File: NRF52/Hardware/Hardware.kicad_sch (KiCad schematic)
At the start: 66 parts, among them J1 USB_C_Receptacle_USB2.0, J2 BAT, J2 LCD, J2 MOTOR, J3 PROG, Q1 AO3401A, Q2 AO3400A, SW1 SW_Push, SW2 SW_Push, SW3 SW_Push, U1 nRF52840, U3 MAX17048, U3 TP4054, U4 XC6206PxxxMR, U5 LSM6DS3, U6 DS3231MZ, U7 W25Q128JVS, Y1 32MHz 8pF ±10ppm, Y2 32.768kHz 6pF ±20ppm

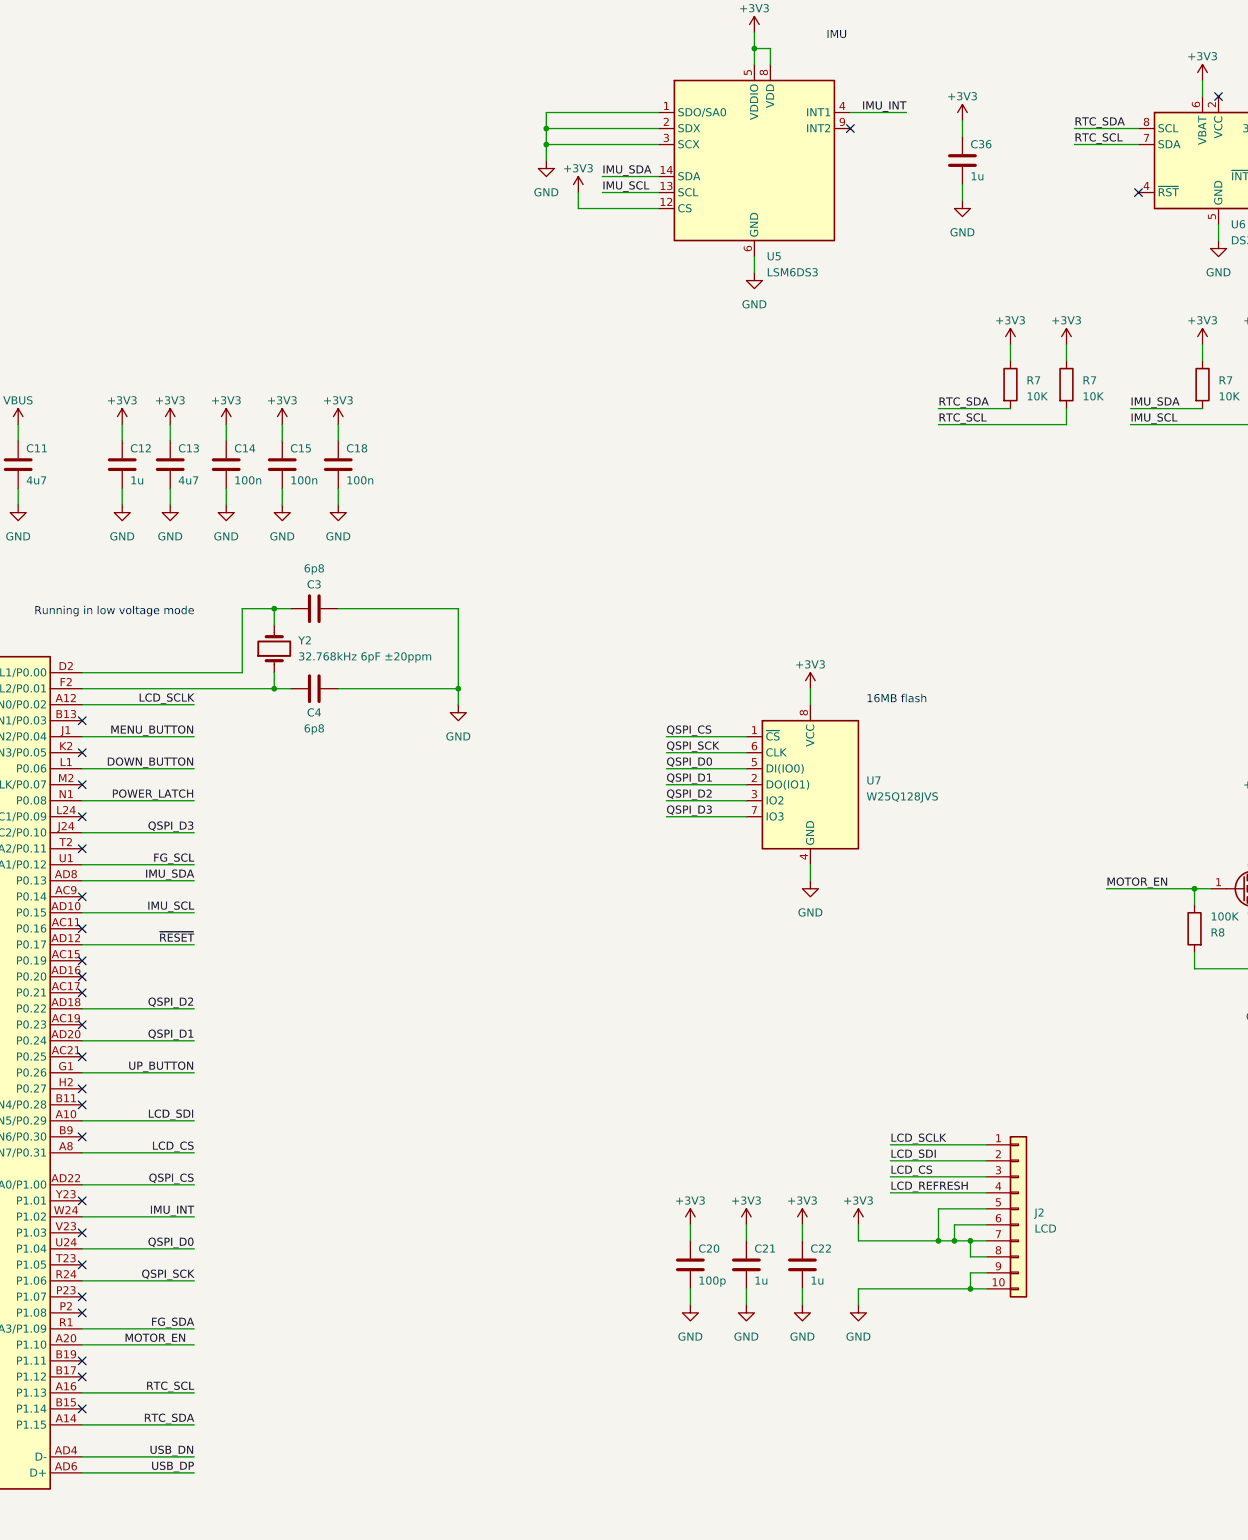
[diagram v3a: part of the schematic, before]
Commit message: Start circuitpython version of software
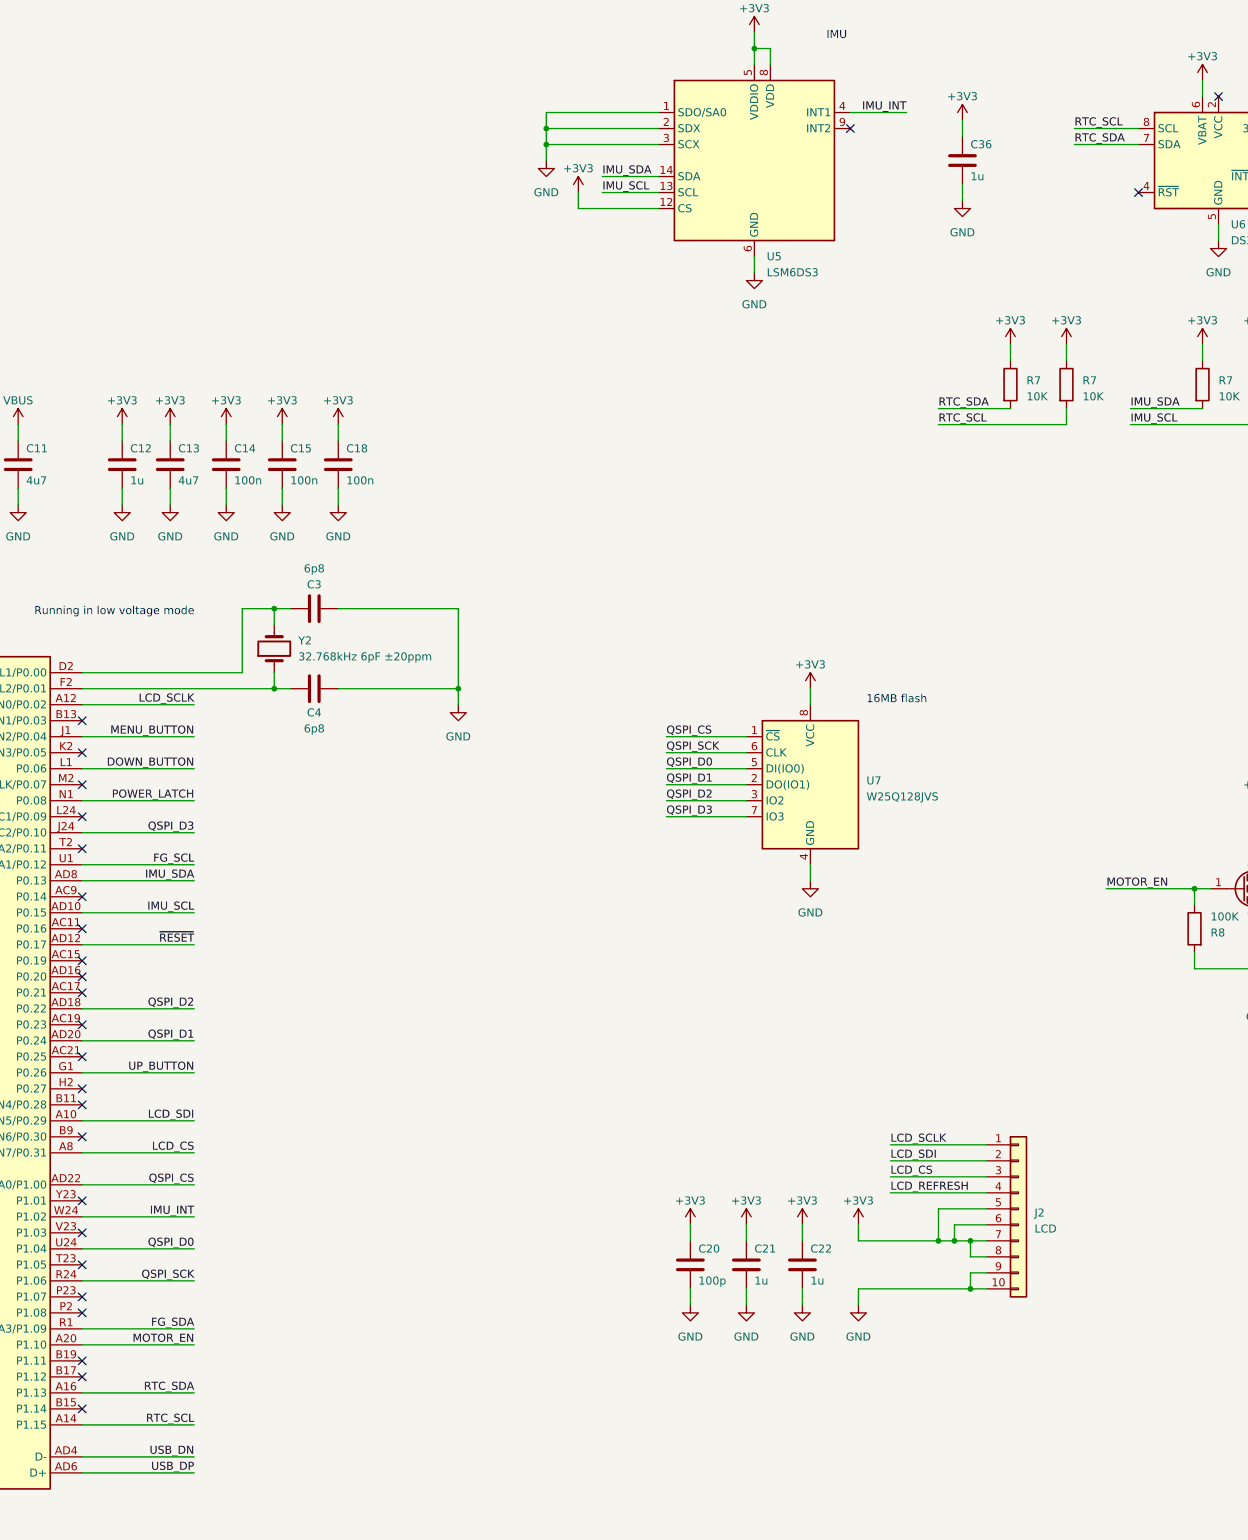
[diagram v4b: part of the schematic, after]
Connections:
- net RTC_SCL: now also U1.A14 (P1.15), U6.8 (SCL); no longer U1.A16 (P1.13), U6.7 (SDA)
- net RTC_SDA: now also U1.A16 (P1.13), U6.7 (SDA); no longer U1.A14 (P1.15), U6.8 (SCL)
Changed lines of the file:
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@@
-    (effects (font (size 1.27 1.27)) (justify left bottom))
-  )
-  (label "RTC_SCL" (at 466.09 123.19 0) (fields_autoplaced)
     (effects (font (size 1.27 1.27)) (justify left bottom))
   )
@@
     (effects (font (size 1.27 1.27)) (justify left bottom))
   )
+  (label "RTC_SDA" (at 326.39 321.31 180) (fields_autoplaced)
+    (effects (font (size 1.27 1.27)) (justify right bottom))
+  )
   (label "MENU_BUTTON" (at 326.39 217.17 180) (fields_autoplaced)
     (effects (font (size 1.27 1.27)) (justify right bottom))
@@
     (effects (font (size 1.27 1.27)) (justify right bottom))
   )
+  (label "RTC_SDA" (at 466.09 123.19 0) (fields_autoplaced)
+    (effects (font (size 1.27 1.27)) (justify left bottom))
+  )
   (label "QSPI_D0" (at 326.39 298.45 180) (fields_autoplaced)
     (effects (font (size 1.27 1.27)) (justify right bottom))
-  )
-  (label "RTC_SDA" (at 466.09 120.65 0) (fields_autoplaced)
-    (effects (font (size 1.27 1.27)) (justify left bottom))
   )
   (label "USB_DN" (at 71.12 41.91 180) (fields_autoplaced)
@@
     (effects (font (size 1.27 1.27)) (justify right bottom))
   )
+  (label "RTC_SCL" (at 466.09 120.65 0) (fields_autoplaced)
+    (effects (font (size 1.27 1.27)) (justify left bottom))
+  )
   (label "UP_BUTTON" (at 326.39 270.51 180) (fields_autoplaced)
     (effects (font (size 1.27 1.27)) (justify right bottom))
@@
     (effects (font (size 1.27 1.27)) (justify right bottom))
   )
-  (label "RTC_SCL" (at 326.39 321.31 180) (fields_autoplaced)
-    (effects (font (size 1.27 1.27)) (justify right bottom))
-  )
   (label "DOWN_BUTTON" (at 87.63 233.68 0) (fields_autoplaced)
     (effects (font (size 1.27 1.27)) (justify left bottom))
   )
-  (label "RTC_SDA" (at 326.39 326.39 180) (fields_autoplaced)
-    (effects (font (size 1.27 1.27)) (justify right bottom))
-  )
-  (label "MOTOR_EN" (at 325.12 313.69 180) (fields_autoplaced)
+  (label "MOTOR_EN" (at 326.39 313.69 180) (fields_autoplaced)
     (effects (font (size 1.27 1.27)) (justify right bottom))
   )
@@
     (effects (font (size 1.27 1.27)) (justify left bottom))
   )
+  (label "RTC_SCL" (at 326.39 326.39 180) (fields_autoplaced)
+    (effects (font (size 1.27 1.27)) (justify right bottom))
+  )
   (label "QSPI_SCK" (at 401.32 219.71 0) (fields_autoplaced)
